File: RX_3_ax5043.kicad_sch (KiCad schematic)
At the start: 19 parts, among them P3 CONUFL001-SMD-T, Q5 DMP2037U-7, U17 AX5043

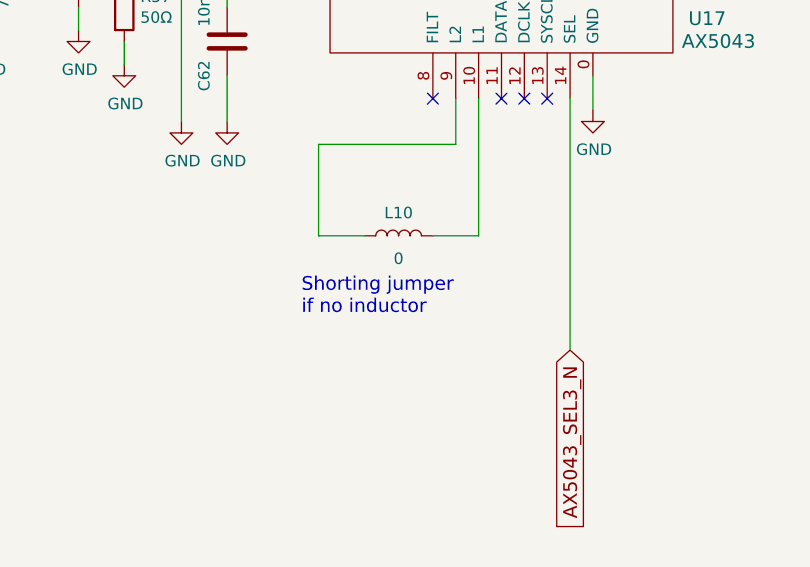
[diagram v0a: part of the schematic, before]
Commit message: Update schematics to match what is done to the boards so far
Get ready to split off a branch where the updates to the board can be
done while still keeping updates for the prototypes.

Signed-off-by: Corey Minyard <corey@minyard.net>
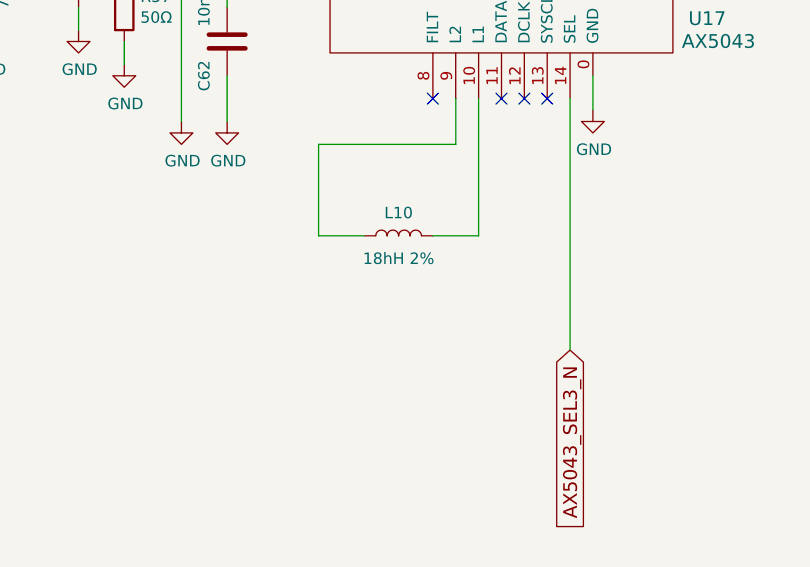
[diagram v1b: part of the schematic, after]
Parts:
- L10: value 0 -> 18hH 2%
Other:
- note removed: "Shorting jumper if no inductor"
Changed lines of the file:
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@@
-		)
-	)
-	(text "Shorting jumper\nif no inductor"
-		(exclude_from_sim no)
-		(at 247.015 172.72 0)
-		(effects
-			(font
-				(size 1.524 1.524)
-			)
-			(justify left bottom)
 		)
 	)
@@
 			)
 		)
-		(property "Value" "0"
+		(property "Value" "18hH 2%"
 			(at 257.81 166.37 90)
 			(effects

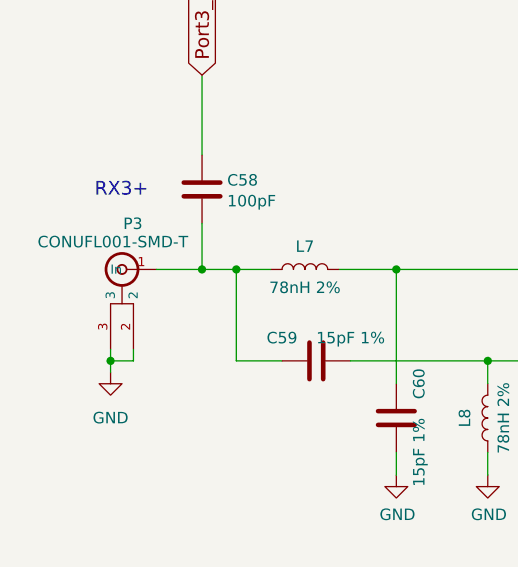
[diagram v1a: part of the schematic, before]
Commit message: Clean up the U.FL connectors a little more
Re-add the ones for TX/RX so both MMCX and U.FL are available.

Move P8 to a better location.

Signed-off-by: Corey Minyard <corey@minyard.net>
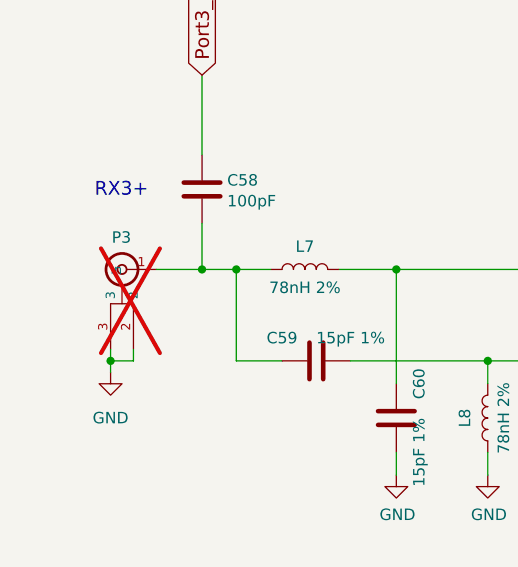
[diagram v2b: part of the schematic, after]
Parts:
- P3: now not fitted; now left out of the parts list
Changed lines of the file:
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@@
 		(unit 1)
 		(exclude_from_sim no)
-		(in_bom yes)
+		(in_bom no)
 		(on_board yes)
-		(dnp no)
+		(dnp yes)
 		(property "Reference" "P3"
-			(at 173.736 113.03 0)
+			(at 172.466 114.554 0)
 			(effects
 				(font
@@
 					(size 1.27 1.27)
 				)
+				(hide yes)
 			)
 		)

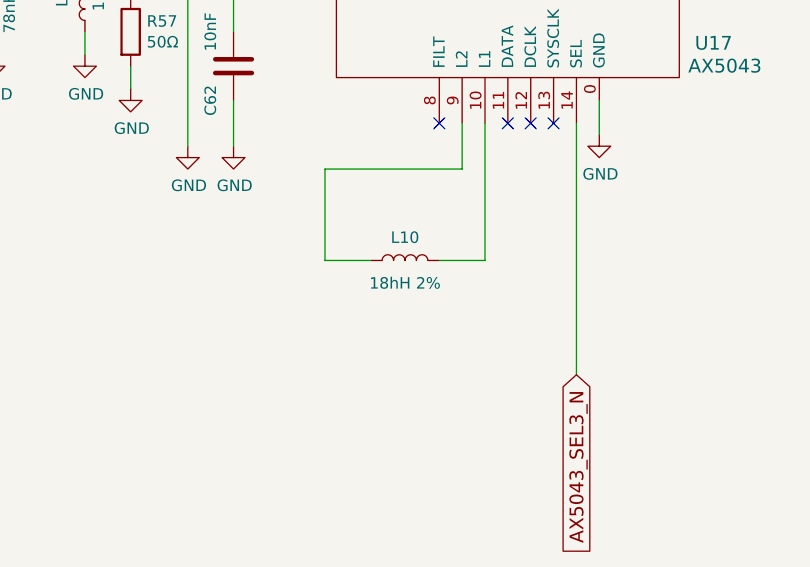
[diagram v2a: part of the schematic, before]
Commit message: Clean up BOM issues
Fix missing parts and mistypes parts.

Signed-off-by: Corey Minyard <corey@minyard.net>
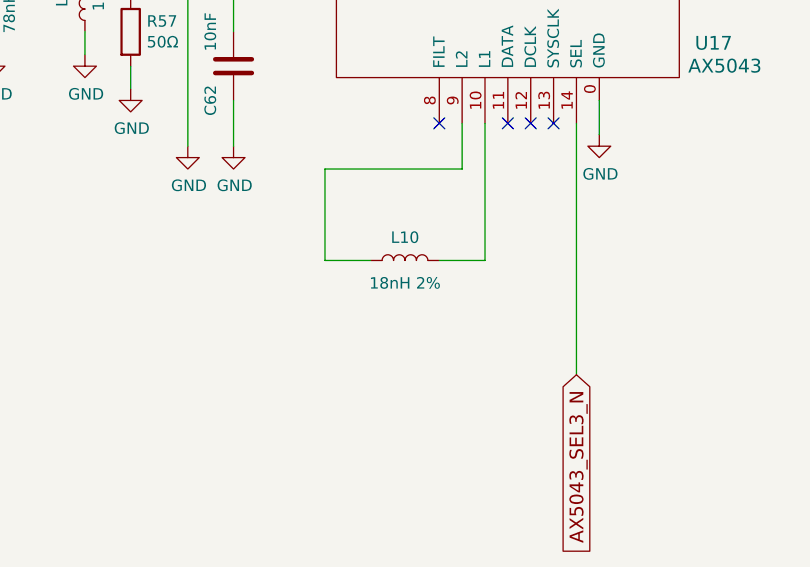
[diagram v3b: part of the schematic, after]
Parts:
- L10: value 18hH 2% -> 18nH 2%
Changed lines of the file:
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@@
 			)
 		)
-		(property "Value" "18hH 2%"
+		(property "Value" "18nH 2%"
 			(at 257.81 166.37 90)
 			(effects

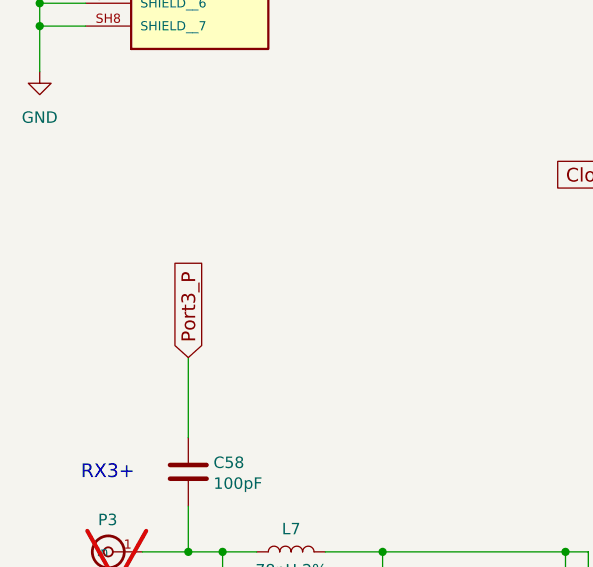
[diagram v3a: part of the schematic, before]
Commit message: Run the extra GPIOs to the PC104
They were recently freed with the ABF rework, use them.

Also, a kicad update broke some stuff, fix it.

Signed-off-by: Corey Minyard <corey@minyard.net>
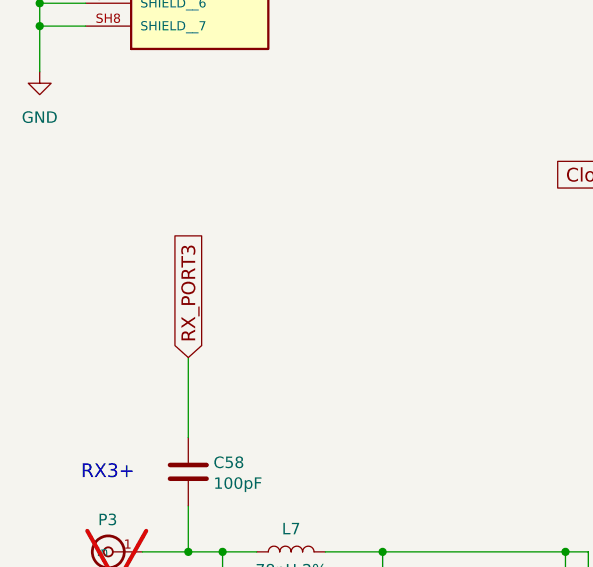
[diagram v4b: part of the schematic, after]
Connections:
- net Port3_P renamed RX_PORT3
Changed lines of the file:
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@@
 		)
 	)
-	(global_label "Port3_P"
+	(global_label "RX_PORT3"
 		(shape input)
 		(at 180.34 96.52 90)
@@
 		)
 		(property "Intersheetrefs" "${INTERSHEET_REFS}"
-			(at 180.34 84.8695 90)
+			(at 180.34 82.3296 90)
 			(effects
 				(font

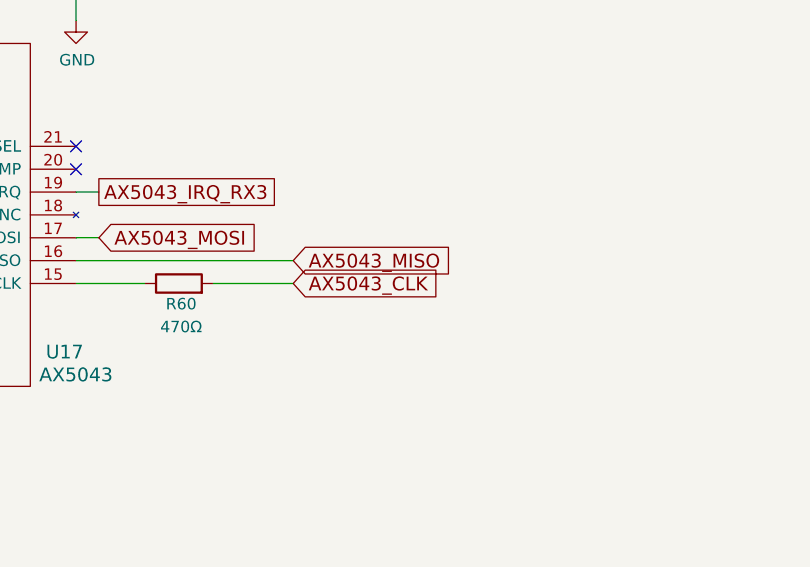
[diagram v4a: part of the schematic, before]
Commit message: Get the board ready for operation
Make the board ready as a final product, remove the lab testing portions
and add in the things required for full operation.

Signed-off-by: Corey Minyard <corey@minyard.net>
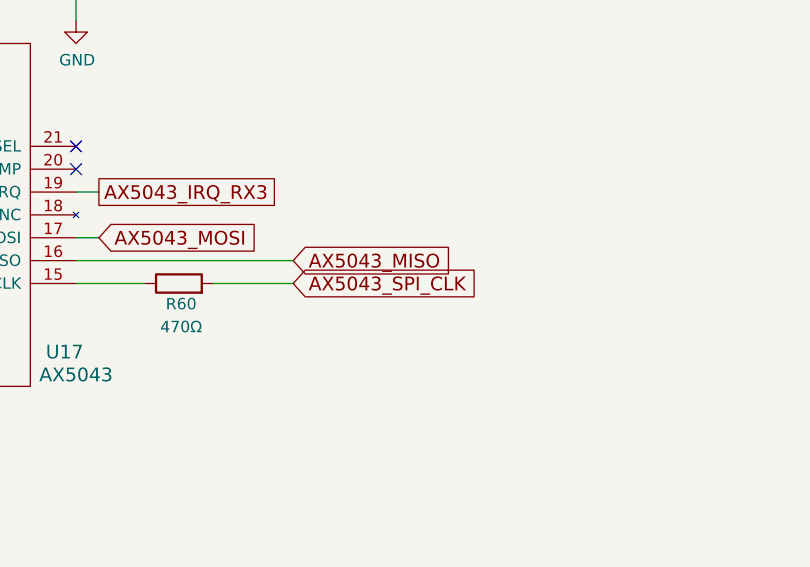
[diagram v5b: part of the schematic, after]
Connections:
- net AX5043_CLK renamed AX5043_SPI_CLK
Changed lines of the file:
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@@
 		)
 	)
-	(global_label "AX5043_CLK"
+	(global_label "AX5043_SPI_CLK"
 		(shape input)
 		(at 317.5 132.08 0)

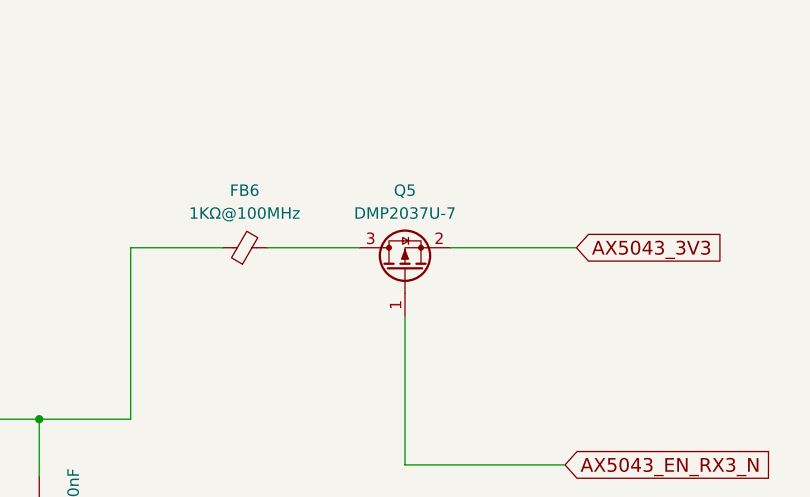
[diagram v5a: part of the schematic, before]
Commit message: Parts replacements for out of stock parts
Signed-off-by: Corey Minyard <corey@minyard.net>
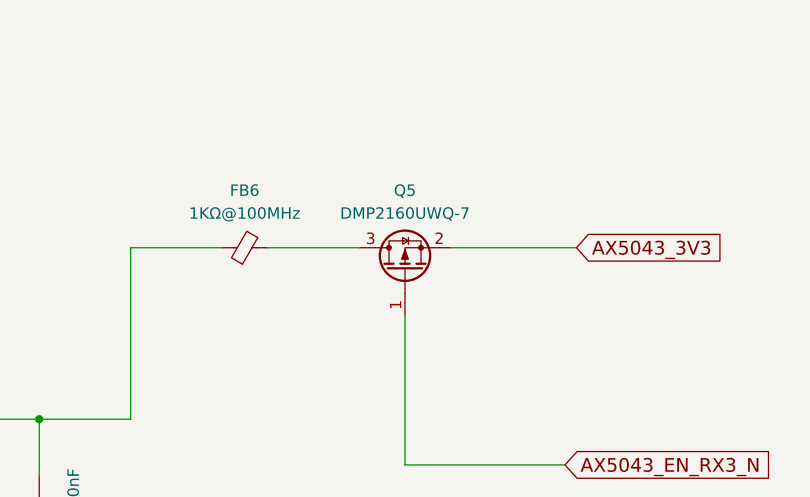
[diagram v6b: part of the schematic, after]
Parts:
- Q5: value DMP2037U-7 -> DMP2160UWQ-7; footprint Package_TO_SOT_SMD:SOT-23 -> Package_TO_SOT_SMD:SOT-323_SC-70
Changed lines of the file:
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@@
+	)
+	(symbol
+		(lib_id "Transistor_FET:Q_PMOS_GSD")
+		(at 334.01 67.31 90)
+		(unit 1)
+		(exclude_from_sim no)
+		(in_bom yes)
+		(on_board yes)
+		(dnp no)
+		(fields_autoplaced yes)
+		(property "Reference" "Q5"
+			(at 334.01 58.42 90)
+			(effects
+				(font
+					(size 1.27 1.27)
+				)
+			)
+		)
+		(property "Value" "DMP2160UWQ-7"
+			(at 334.01 60.96 90)
+			(effects
+				(font
+					(size 1.27 1.27)
+				)
+			)
+		)
+		(property "Footprint" "Package_TO_SOT_SMD:SOT-323_SC-70"
+			(at 331.47 62.23 0)
+			(effects
+				(font
+					(size 1.27 1.27)
+				)
+				(hide yes)
+			)
+		)
+		(property "Datasheet" "~"
+			(at 334.01 67.31 0)
+			(effects
+				(font
+					(size 1.27 1.27)
+				)
+				(hide yes)
+			)
+		)
+		(property "Description" "P-MOSFET transistor, gate/source/drain"
+			(at 334.01 67.31 0)
+			(effects
+				(font
+					(size 1.27 1.27)
+				)
+				(hide yes)
+			)
+		)
+		(pin "2"
+		)
+		(pin "1"
+		)
+		(pin "3"
+		)
+		(instances
+			(project "PacSat_AFSK"
+				(path "/cc9f42d2-6985-41ac-acab-5ab7b01c5b38/d9a83ee4-3280-49b9-88b8-54d26cbd8ed1/6f28879f-0500-4efd-92c5-41e4c690888d"
+					(reference "Q5")
+					(unit 1)
+				)
+			)
+		)
 	)
 	(symbol
@@
 					(unit 1)
 				)
-			)
-		)
-	)
-	(symbol
-		(lib_id "Transistor_FET:Q_PMOS_GSD")
-		(at 334.01 67.31 90)
-		(unit 1)
-		(exclude_from_sim no)
-		(in_bom yes)
-		(on_board yes)
-		(dnp no)
-		(fields_autoplaced yes)
-		(property "Reference" "Q5"
-			(at 334.01 58.42 90)
-			(effects
-				(font
-					(size 1.27 1.27)
-				)
-			)
-		)
-		(property "Value" "DMP2037U-7"
-			(at 334.01 60.96 90)
-			(effects
-				(font
-					(size 1.27 1.27)
-				)
-			)
-		)
-		(property "Footprint" "Package_TO_SOT_SMD:SOT-23"
-			(at 331.47 62.23 0)
-			(effects
-				(font
-					(size 1.27 1.27)
-				)
-				(hide yes)
-			)
-		)
-		(property "Datasheet" "~"
-			(at 334.01 67.31 0)
-			(effects
-				(font
-					(size 1.27 1.27)
-				)
-				(hide yes)
-			)
-		)
-		(property "Description" "P-MOSFET transistor, gate/source/drain"
-			(at 334.01 67.31 0)
-			(effects
-				(font
-					(size 1.27 1.27)
-				)
-				(hide yes)
-			)
-		)
-		(pin "2"
-		)
-		(pin "1"
-		)
-		(pin "3"
-		)
-		(instances
-			(project "PacSat_AFSK"
-				(path "/cc9f42d2-6985-41ac-acab-5ab7b01c5b38/d9a83ee4-3280-49b9-88b8-54d26cbd8ed1/6f28879f-0500-4efd-92c5-41e4c690888d"
-					(reference "Q5")
-					(unit 1)
-				)
